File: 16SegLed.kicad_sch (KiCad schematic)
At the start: 30 parts, among them J1 Conn_01x10, J2 Conn_01x10, J3 Conn_01x10, J4 Conn_01x06_Socket, J5 Conn_01x04_Pin, J6 Conn_01x04_Pin, SW1 SW_Push, SW2 SW_Push, U1 ESP32-S3-WROOM-1, U2 AMS1117-3.3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

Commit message: Add QR code for repository @ github
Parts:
- added FID1: Fiducial, ProjectLibrary:QR-Code, symbol Mechanical:Fiducial
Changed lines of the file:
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@@
+    )
+  )
+  (symbol (lib_id "Mechanical:Fiducial") (at 19.685 167.005 0) (unit 1)
+    (in_bom yes) (on_board yes) (dnp no) (fields_autoplaced)
+    (property "Reference" "FID1" (at 22.86 165.735 0)
+      (effects (font (size 1.27 1.27)) (justify left))
+    )
+    (property "Value" "Fiducial" (at 22.86 168.275 0)
+      (effects (font (size 1.27 1.27)) (justify left))
+    )
+    (property "Footprint" "ProjectLibrary:QR-Code" (at 19.685 167.005 0)
+      (effects (font (size 1.27 1.27)) hide)
+    )
+    (property "Datasheet" "~" (at 19.685 167.005 0)
+      (effects (font (size 1.27 1.27)) hide)
+    )
+    (instances
+      (project "16SegLed"
+        (path "/41dad044-0879-44f7-af2f-de3faef8859f"
+          (reference "FID1") (unit 1)
+        )
+      )
     )
   )

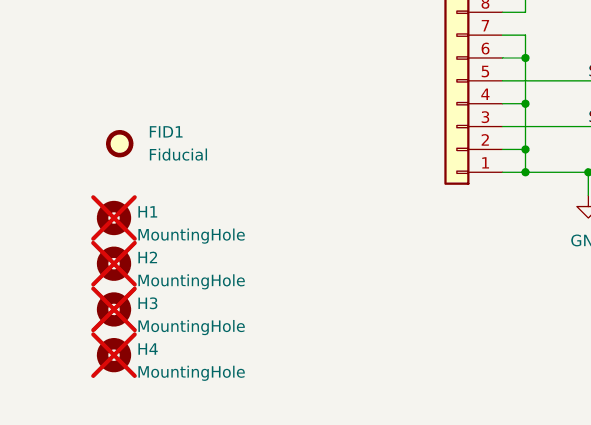
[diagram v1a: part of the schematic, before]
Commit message: Connect mounting holes to ground
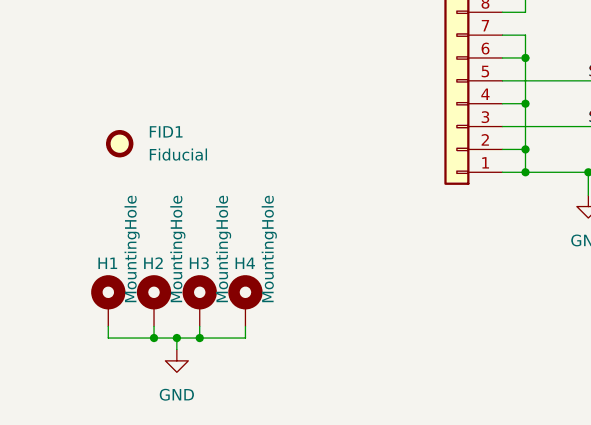
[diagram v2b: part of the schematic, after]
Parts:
- H1, H2, H3, H4: symbol Mechanical:MountingHole -> Mechanical:MountingHole_Pad; now fitted; now in the parts list
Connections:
- net GND: now also H1.1, H2.1, H3.1, H4.1
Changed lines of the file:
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@@
   (junction (at 71.755 170.18) (diameter 0) (color 0 0 0 0)
   )
+  (junction (at 23.495 188.595) (diameter 0) (color 0 0 0 0)
+  )
   (junction (at 221.615 83.185) (diameter 0) (color 0 0 0 0)
   )
@@
   (junction (at 247.015 -29.845) (diameter 0) (color 0 0 0 0)
   )
+  (junction (at 26.035 188.595) (diameter 0) (color 0 0 0 0)
+  )
   (junction (at 238.125 130.175) (diameter 0) (color 0 0 0 0)
   )
@@
   )
   (junction (at 266.065 130.175) (diameter 0) (color 0 0 0 0)
+  )
+  (junction (at 28.575 188.595) (diameter 0) (color 0 0 0 0)
   )
   (junction (at 175.26 -29.845) (diameter 0) (color 0 0 0 0)
@@
     (stroke (width 0) (type default))
   )
+  (wire (pts (xy 18.415 188.595) (xy 23.495 188.595))
+    (stroke (width 0) (type default))
+  )
   (wire (pts (xy 124.46 26.035) (xy 121.92 26.035))
     (stroke (width 0) (type default))
@@
     (stroke (width 0) (type default))
   )
+  (wire (pts (xy 26.035 188.595) (xy 28.575 188.595))
+    (stroke (width 0) (type default))
+  )
   (wire (pts (xy 79.375 157.48) (xy 79.375 162.56))
     (stroke (width 0) (type default))
@@
     (stroke (width 0) (type default))
   )
+  (wire (pts (xy 28.575 188.595) (xy 28.575 187.325))
+    (stroke (width 0) (type default))
+  )
   (wire (pts (xy 184.785 135.89) (xy 167.64 135.89))
     (stroke (width 0) (type default))
@@
     (stroke (width 0) (type default))
   )
+  (wire (pts (xy 33.655 188.595) (xy 33.655 187.325))
+    (stroke (width 0) (type default))
+  )
   (wire (pts (xy 167.64 138.43) (xy 180.34 138.43))
     (stroke (width 0) (type default))
@@
     (stroke (width 0) (type default))
   )
+  (wire (pts (xy 23.495 188.595) (xy 26.035 188.595))
+    (stroke (width 0) (type default))
+  )
   (wire (pts (xy 151.765 178.435) (xy 156.845 178.435))
     (stroke (width 0) (type default))
@@
     (stroke (width 0) (type default))
   )
+  (wire (pts (xy 28.575 188.595) (xy 33.655 188.595))
+    (stroke (width 0) (type default))
+  )
   (wire (pts (xy 284.48 -33.02) (xy 283.21 -33.02))
     (stroke (width 0) (type default))
@@
     (stroke (width 0) (type default))
   )
+  (wire (pts (xy 26.035 189.865) (xy 26.035 188.595))
+    (stroke (width 0) (type default))
+  )
   (wire (pts (xy 175.26 -29.845) (xy 175.26 -17.145))
     (stroke (width 0) (type default))
@@
     (stroke (width 0) (type default))
   )
+  (wire (pts (xy 18.415 188.595) (xy 18.415 187.325))
+    (stroke (width 0) (type default))
+  )
   (wire (pts (xy 160.02 95.885) (xy 156.845 95.885))
     (stroke (width 0) (type default))
   )
   (wire (pts (xy 179.07 125.095) (xy 180.34 125.095))
+    (stroke (width 0) (type default))
+  )
+  (wire (pts (xy 23.495 188.595) (xy 23.495 187.325))
     (stroke (width 0) (type default))
   )
@@
         (path "/41dad044-0879-44f7-af2f-de3faef8859f"
           (reference "#PWR014") (unit 1)
+        )
+      )
+    )
+  )
+  (symbol (lib_id "power:GND") (at 26.035 189.865 0) (unit 1)
+    (in_bom yes) (on_board yes) (dnp no) (fields_autoplaced)
+    (property "Reference" "#PWR040" (at 26.035 196.215 0)
+      (effects (font (size 1.27 1.27)) hide)
+    )
+    (property "Value" "GND" (at 26.035 194.945 0)
+      (effects (font (size 1.27 1.27)))
+    )
+    (property "Footprint" "" (at 26.035 189.865 0)
+      (effects (font (size 1.27 1.27)) hide)
+    )
+    (property "Datasheet" "" (at 26.035 189.865 0)
+      (effects (font (size 1.27 1.27)) hide)
+    )
+    (pin "1")
+    (instances
+      (project "16SegLed"
+        (path "/41dad044-0879-44f7-af2f-de3faef8859f"
+          (reference "#PWR040") (unit 1)
         )
       )
@@
     )
   )
-  (symbol (lib_id "Mechanical:MountingHole") (at 19.05 190.5 0) (unit 1)
-    (in_bom no) (on_board yes) (dnp yes) (fields_autoplaced)
-    (property "Reference" "H4" (at 21.59 189.865 0)
-      (effects (font (size 1.27 1.27)) (justify left))
-    )
-    (property "Value" "MountingHole" (at 21.59 192.405 0)
-      (effects (font (size 1.27 1.27)) (justify left))
-    )
-    (property "Footprint" "MountingHole:MountingHole_3.2mm_M3_Pad" (at 19.05 190.5 0)
-      (effects (font (size 1.27 1.27)) hide)
-    )
-    (property "Datasheet" "~" (at 19.05 190.5 0)
-      (effects (font (size 1.27 1.27)) hide)
-    )
+  (symbol (lib_id "Mechanical:MountingHole_Pad") (at 33.655 184.785 0) (unit 1)
+    (in_bom yes) (on_board yes) (dnp no)
+    (property "Reference" "H4" (at 32.385 180.34 0)
+      (effects (font (size 1.27 1.27)) (justify left))
+    )
+    (property "Value" "MountingHole" (at 36.195 184.785 90)
+      (effects (font (size 1.27 1.27)) (justify left))
+    )
+    (property "Footprint" "MountingHole:MountingHole_3.2mm_M3_Pad" (at 33.655 184.785 0)
+      (effects (font (size 1.27 1.27)) hide)
+    )
+    (property "Datasheet" "~" (at 33.655 184.785 0)
+      (effects (font (size 1.27 1.27)) hide)
+    )
+    (pin "1")
     (instances
       (project "16SegLed"
@@
     )
   )
-  (symbol (lib_id "Mechanical:MountingHole") (at 19.05 180.34 0) (unit 1)
-    (in_bom no) (on_board yes) (dnp yes) (fields_autoplaced)
-    (property "Reference" "H2" (at 21.59 179.705 0)
-      (effects (font (size 1.27 1.27)) (justify left))
-    )
-    (property "Value" "MountingHole" (at 21.59 182.245 0)
-      (effects (font (size 1.27 1.27)) (justify left))
-    )
-    (property "Footprint" "MountingHole:MountingHole_3.2mm_M3_Pad" (at 19.05 180.34 0)
-      (effects (font (size 1.27 1.27)) hide)
-    )
-    (property "Datasheet" "~" (at 19.05 180.34 0)
-      (effects (font (size 1.27 1.27)) hide)
-    )
+  (symbol (lib_id "Mechanical:MountingHole_Pad") (at 23.495 184.785 0) (unit 1)
+    (in_bom yes) (on_board yes) (dnp no)
+    (property "Reference" "H2" (at 22.225 180.34 0)
+      (effects (font (size 1.27 1.27)) (justify left))
+    )
+    (property "Value" "MountingHole" (at 26.035 184.785 90)
+      (effects (font (size 1.27 1.27)) (justify left))
+    )
+    (property "Footprint" "MountingHole:MountingHole_3.2mm_M3_Pad" (at 23.495 184.785 0)
+      (effects (font (size 1.27 1.27)) hide)
+    )
+    (property "Datasheet" "~" (at 23.495 184.785 0)
+      (effects (font (size 1.27 1.27)) hide)
+    )
+    (pin "1")
     (instances
       (project "16SegLed"
@@
     )
   )
-  (symbol (lib_id "Mechanical:MountingHole") (at 19.05 175.26 0) (unit 1)
-    (in_bom no) (on_board yes) (dnp yes) (fields_autoplaced)
-    (property "Reference" "H1" (at 21.59 174.625 0)
-      (effects (font (size 1.27 1.27)) (justify left))
-    )
-    (property "Value" "MountingHole" (at 21.59 177.165 0)
-      (effects (font (size 1.27 1.27)) (justify left))
-    )
-    (property "Footprint" "MountingHole:MountingHole_3.2mm_M3_Pad" (at 19.05 175.26 0)
-      (effects (font (size 1.27 1.27)) hide)
-    )
-    (property "Datasheet" "~" (at 19.05 175.26 0)
-      (effects (font (size 1.27 1.27)) hide)
-    )
+  (symbol (lib_id "Mechanical:MountingHole_Pad") (at 18.415 184.785 0) (unit 1)
+    (in_bom yes) (on_board yes) (dnp no)
+    (property "Reference" "H1" (at 17.145 180.34 0)
+      (effects (font (size 1.27 1.27)) (justify left))
+    )
+    (property "Value" "MountingHole" (at 20.955 184.785 90)
+      (effects (font (size 1.27 1.27)) (justify left))
+    )
+    (property "Footprint" "MountingHole:MountingHole_3.2mm_M3_Pad" (at 18.415 184.785 0)
+      (effects (font (size 1.27 1.27)) hide)
+    )
+    (property "Datasheet" "~" (at 18.415 184.785 0)
+      (effects (font (size 1.27 1.27)) hide)
+    )
+    (pin "1")
     (instances
       (project "16SegLed"
@@
     )
   )
-  (symbol (lib_id "Mechanical:MountingHole") (at 19.05 185.42 0) (unit 1)
-    (in_bom no) (on_board yes) (dnp yes) (fields_autoplaced)
-    (property "Reference" "H3" (at 21.59 184.785 0)
-      (effects (font (size 1.27 1.27)) (justify left))
-    )
-    (property "Value" "MountingHole" (at 21.59 187.325 0)
-      (effects (font (size 1.27 1.27)) (justify left))
-    )
-    (property "Footprint" "MountingHole:MountingHole_3.2mm_M3_Pad" (at 19.05 185.42 0)
-      (effects (font (size 1.27 1.27)) hide)
-    )
-    (property "Datasheet" "~" (at 19.05 185.42 0)
-      (effects (font (size 1.27 1.27)) hide)
-    )
-    (instances
-      (project "16SegLed"
+  (symbol (lib_id "Mechanical:MountingHole_Pad") (at 28.575 184.785 0) (unit 1)
+    (in_bom yes) (on_board yes) (dnp no)
+    (property "Reference" "H3" (at 27.305 180.34 0)
+      (effects (font (size 1.27 1.27)) (justify left))
+    )
+    (property "Value" "MountingHole" (at 31.115 184.785 90)
+      (effects (font (size 1.27 1.27)) (justify left))
+    )
+    (property "Footprint" "MountingHole:MountingHole_3.2mm_M3_Pad" (at 28.575 184.785 0)
+      (effects (font (size 1.27 1.27)) hide)
+    )
+    (property "Datasheet" "~" (at 28.575 184.785 0)
+      (effects (font (size 1.27 1.27)) hide)
+    )
+    (pin "1")
+    (instances
+      (project "16SegLed"

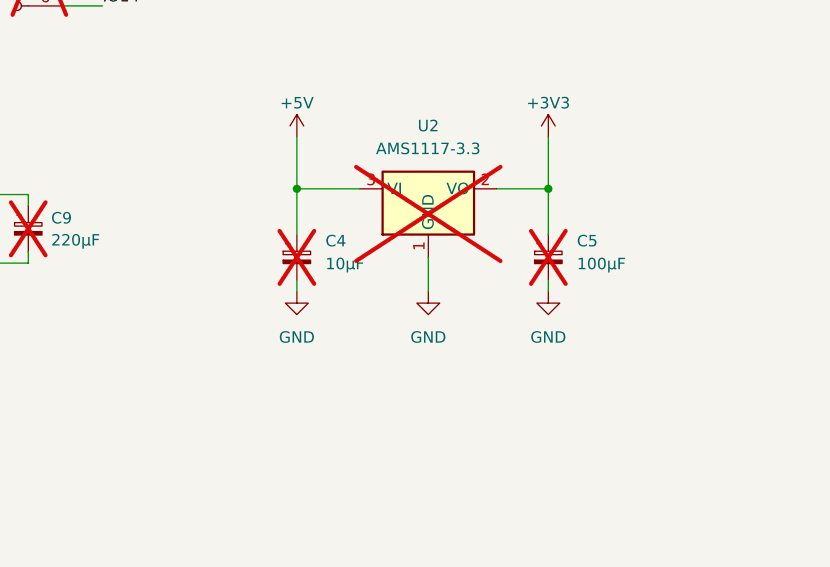
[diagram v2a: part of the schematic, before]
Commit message: Fix 3.3 V regulator circuit
- Use polarized footprints for tantalum capacitors
- Add 100nF at input and output of AMS1117
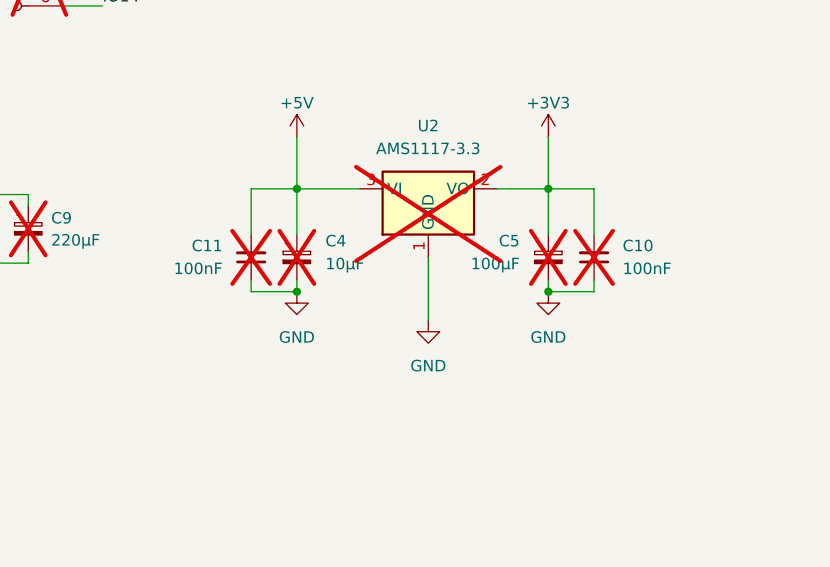
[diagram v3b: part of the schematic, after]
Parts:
- added C10, C11: 100nF, Capacitor_SMD:C_0805_2012Metric, symbol Device:C_Small
- C4, C5: footprint Capacitor_SMD:C_1206_3216Metric -> Capacitor_Tantalum_SMD:CP_EIA-3216-10_Kemet-I
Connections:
- net +3V3: now also C10.2
- net +5V: now also C11.2
- net GND: now also C10.1, C11.1
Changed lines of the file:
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@@
 (kicad_sch (version 20230121) (generator eeschema)
   (paper "A4")
+  (junction (at 238.125 141.605) (diameter 0) (color 0 0 0 0)
+  )
   (junction (at 180.34 146.05) (diameter 0) (color 0 0 0 0)
   )
@@
   )
   (junction (at 79.375 170.18) (diameter 0) (color 0 0 0 0)
+  )
+  (junction (at 266.065 141.605) (diameter 0) (color 0 0 0 0)
   )
   (junction (at 36.83 53.975) (diameter 0) (color 0 0 0 0)
@@
     (stroke (width 0) (type default))
   )
+  (wire (pts (xy 266.065 130.175) (xy 271.145 130.175))
+    (stroke (width 0) (type default))
+  )
   (wire (pts (xy 238.125 130.175) (xy 238.125 135.255))
     (stroke (width 0) (type default))
@@
     (stroke (width 0) (type default))
   )
-  (wire (pts (xy 252.73 141.605) (xy 252.73 137.795))
-    (stroke (width 0) (type default))
-  )
   (wire (pts (xy 266.065 124.46) (xy 266.065 130.175))
     (stroke (width 0) (type default))
@@
     (stroke (width 0) (type default))
   )
+  (wire (pts (xy 266.065 141.605) (xy 271.145 141.605))
+    (stroke (width 0) (type default))
+  )
   (wire (pts (xy 253.365 31.75) (xy 250.19 31.75))
     (stroke (width 0) (type default))
@@
     (stroke (width 0) (type default))
   )
+  (wire (pts (xy 271.145 140.335) (xy 271.145 141.605))
+    (stroke (width 0) (type default))
+  )
   (wire (pts (xy 179.07 92.075) (xy 183.515 92.075))
     (stroke (width 0) (type default))
@@
     (stroke (width 0) (type default))
   )
+  (wire (pts (xy 271.145 130.175) (xy 271.145 135.255))
+    (stroke (width 0) (type default))
+  )
   (wire (pts (xy 121.92 180.975) (xy 121.285 180.975))
     (stroke (width 0) (type default))
@@
     (stroke (width 0) (type default))
   )
+  (wire (pts (xy 233.045 141.605) (xy 238.125 141.605))
+    (stroke (width 0) (type default))
+  )
   (wire (pts (xy 167.005 78.105) (xy 167.005 83.185))
     (stroke (width 0) (type default))
@@
     (stroke (width 0) (type default))
   )
+  (wire (pts (xy 252.73 137.795) (xy 252.73 144.78))
+    (stroke (width 0) (type default))
+  )
   (wire (pts (xy 179.07 104.775) (xy 183.515 104.775))
     (stroke (width 0) (type default))
@@
     (stroke (width 0) (type default))
   )
-  (wire (pts (xy 245.11 130.175) (xy 238.125 130.175))
+  (wire (pts (xy 238.125 130.175) (xy 245.11 130.175))
     (stroke (width 0) (type default))
   )
@@
     (stroke (width 0) (type default))
   )
+  (wire (pts (xy 233.045 130.175) (xy 233.045 135.255))
+    (stroke (width 0) (type default))
+  )
   (wire (pts (xy 247.015 -27.94) (xy 247.015 -29.845))
     (stroke (width 0) (type default))
@@
     (stroke (width 0) (type default))
   )
+  (wire (pts (xy 238.125 130.175) (xy 233.045 130.175))
+    (stroke (width 0) (type default))
+  )
   (wire (pts (xy 64.77 149.86) (xy 62.23 149.86))
     (stroke (width 0) (type default))
@@
   )
   (wire (pts (xy 111.125 119.38) (xy 111.125 116.205))
+    (stroke (width 0) (type default))
+  )
+  (wire (pts (xy 233.045 140.335) (xy 233.045 141.605))
     (stroke (width 0) (type default))
   )
@@
     (effects (font (size 1.27 1.27)) (justify left bottom))
   )
-  (netclass_flag "" (length 2.54) (shape round) (at 252.73 139.7 270)
-    (effects (font (size 1.27 1.27)) (justify right bottom))
-    (property "Netclass" "Power" (at 255.905 139.065 0)
-      (effects (font (size 1.27 1.27) italic) (justify left))
+  (netclass_flag "" (length 2.54) (shape round) (at 252.73 142.24 90)
+    (effects (font (size 1.27 1.27)) (justify left bottom))
+    (property "Netclass" "Power" (at 249.555 142.875 0)
+      (effects (font (size 1.27 1.27) italic) (justify right))
     )
   )
@@
       (effects (font (size 1.27 1.27)) (justify left))
     )
-    (property "Footprint" "Capacitor_SMD:C_1206_3216Metric" (at 238.125 137.795 0)
+    (property "Footprint" "Capacitor_Tantalum_SMD:CP_EIA-3216-10_Kemet-I" (at 238.125 137.795 0)
       (effects (font (size 1.27 1.27)) hide)
     )
@@
     )
   )
-  (symbol (lib_id "power:GND") (at 252.73 141.605 0) (unit 1)
-    (in_bom yes) (on_board yes) (dnp no) (fields_autoplaced)
-    (property "Reference" "#PWR013" (at 252.73 147.955 0)
-      (effects (font (size 1.27 1.27)) hide)
-    )
-    (property "Value" "GND" (at 252.73 146.685 0)
-      (effects (font (size 1.27 1.27)))
-    )
-    (property "Footprint" "" (at 252.73 141.605 0)
-      (effects (font (size 1.27 1.27)) hide)
-    )
-    (property "Datasheet" "" (at 252.73 141.605 0)
+  (symbol (lib_id "power:GND") (at 252.73 144.78 0) (unit 1)
+    (in_bom yes) (on_board yes) (dnp no) (fields_autoplaced)
+    (property "Reference" "#PWR013" (at 252.73 151.13 0)
+      (effects (font (size 1.27 1.27)) hide)
+    )
+    (property "Value" "GND" (at 252.73 149.86 0)
+      (effects (font (size 1.27 1.27)))
+    )
+    (property "Footprint" "" (at 252.73 144.78 0)
+      (effects (font (size 1.27 1.27)) hide)
+    )
+    (property "Datasheet" "" (at 252.73 144.78 0)
       (effects (font (size 1.27 1.27)) hide)
     )
@@
         (path "/41dad044-0879-44f7-af2f-de3faef8859f"
           (reference "#PWR010") (unit 1)
+        )
+      )
+    )
+  )
+  (symbol (lib_id "Device:C_Small") (at 233.045 137.795 0) (mirror x) (unit 1)
+    (in_bom yes) (on_board yes) (dnp yes)
+    (property "Reference" "C11" (at 229.87 136.5186 0)
+      (effects (font (size 1.27 1.27)) (justify right))
+    )
+    (property "Value" "100nF" (at 229.87 139.0586 0)
+      (effects (font (size 1.27 1.27)) (justify right))
+    )
+    (property "Footprint" "Capacitor_SMD:C_0805_2012Metric" (at 233.045 137.795 0)
+      (effects (font (size 1.27 1.27)) hide)
+    )
+    (property "Datasheet" "https://datasheet.lcsc.com/lcsc/2207221830_FH--Guangdong-Fenghua-Advanced-Tech-0805B104K250NT_C5120075.pdf" (at 233.045 137.795 0)
+      (effects (font (size 1.27 1.27)) hide)
+    )
+    (property "LCSC" "C5120075" (at 233.045 137.795 0)
+      (effects (font (size 1.27 1.27)) hide)
+    )
+    (pin "1")
+    (pin "2")
+    (instances
+      (project "16SegLed"
+        (path "/41dad044-0879-44f7-af2f-de3faef8859f"
+          (reference "C11") (unit 1)
         )
       )
@@
     )
   )
-  (symbol (lib_id "Device:C_Polarized_Small") (at 266.065 137.795 0) (unit 1)
-    (in_bom yes) (on_board yes) (dnp yes) (fields_autoplaced)
-    (property "Reference" "C5" (at 269.24 135.9789 0)
-      (effects (font (size 1.27 1.27)) (justify left))
-    )
-    (property "Value" "100µF" (at 269.24 138.5189 0)
-      (effects (font (size 1.27 1.27)) (justify left))
-    )
-    (property "Footprint" "Capacitor_SMD:C_1206_3216Metric" (at 266.065 137.795 0)
+  (symbol (lib_id "Device:C_Polarized_Small") (at 266.065 137.795 0) (mirror y) (unit 1)
+    (in_bom yes) (on_board yes) (dnp yes)
+    (property "Reference" "C5" (at 262.89 135.9789 0)
+      (effects (font (size 1.27 1.27)) (justify left))
+    )
+    (property "Value" "100µF" (at 262.89 138.5189 0)
+      (effects (font (size 1.27 1.27)) (justify left))
+    )
+    (property "Footprint" "Capacitor_Tantalum_SMD:CP_EIA-3216-10_Kemet-I" (at 266.065 137.795 0)
       (effects (font (size 1.27 1.27)) hide)
     )
@@
         )
       )
+    )
+  )
+  (symbol (lib_id "Device:C_Small") (at 271.145 137.795 180) (unit 1)
+    (in_bom yes) (on_board yes) (dnp yes)
+    (property "Reference" "C10" (at 274.32 136.5186 0)
+      (effects (font (size 1.27 1.27)) (justify right))
+    )
+    (property "Value" "100nF" (at 274.32 139.0586 0)
+      (effects (font (size 1.27 1.27)) (justify right))
+    )
+    (property "Footprint" "Capacitor_SMD:C_0805_2012Metric" (at 271.145 137.795 0)
+      (effects (font (size 1.27 1.27)) hide)
+    )
+    (property "Datasheet" "https://datasheet.lcsc.com/lcsc/2207221830_FH--Guangdong-Fenghua-Advanced-Tech-0805B104K250NT_C5120075.pdf" (at 271.145 137.795 0)
+      (effects (font (size 1.27 1.27)) hide)
+    )
+    (property "LCSC" "C5120075" (at 271.145 137.795 0)
+      (effects (font (size 1.27 1.27)) hide)
+    )
+    (pin "1")
+    (pin "2")
+    (instances
+      (project "16SegLed"
+        (path "/41dad044-0879-44f7-af2f-de3faef8859f"
+          (reference "C10") (unit 1)
+        )
+      )
